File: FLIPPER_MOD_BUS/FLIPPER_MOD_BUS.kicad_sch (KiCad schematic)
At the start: 15 parts, among them J1 Conn_01x02, J2 Conn_01x10_Socket, J3 Conn_01x08_Socket, U1 SP3485EN

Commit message: Flipper Mod Bus Silkcscreen Updated
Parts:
- removed D1: LED_Small, LED_SMD:LED_0603_1608Metric_Pad1.05x0.95mm_HandSolder, symbol Device:LED_Small
- removed R8: 1K, Resistor_SMD:R_0603_1608Metric_Pad0.98x0.95mm_HandSolder, symbol Device:R_Small
- C2: LCSC# (none) -> C14663; Proveedor MOUSER -> LCSC; manf# 0603F104Z160CT -> (none)
- J1: manf# --- -> TRT-02
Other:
- company: (none) -> Electronic Cats
- title: (none) -> Flippe ModBus
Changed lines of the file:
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@@
 (kicad_sch (version 20230121) (generator eeschema)
   (paper "A4")
+  (title_block
+    (title "Flippe ModBus")
+    (date "2024-01-22")
+    (rev "1.0")
+    (company "Electronic Cats")
+    (comment 1 "Roberto Arellano")
+  )
   (junction (at 26.67 23.622) (diameter 0) (color 0 0 0 0)
   )
@@
   (no_connect (at 45.72 94.996))
   (no_connect (at 45.72 100.076))
-  (wire (pts (xy 165.354 39.624) (xy 165.354 45.466))
-    (stroke (width 0) (type default))
-  )
   (wire (pts (xy 32.004 25.908) (xy 32.004 23.622))
     (stroke (width 0) (type default))
@@
     (stroke (width 0) (type default))
   )
-  (wire (pts (xy 165.354 19.558) (xy 165.354 23.876))
-    (stroke (width 0) (type default))
-  )
   (wire (pts (xy 130.556 27.178) (xy 125.476 27.178))
     (stroke (width 0) (type default))
@@
   )
   (wire (pts (xy 21.336 23.622) (xy 26.67 23.622))
-    (stroke (width 0) (type default))
-  )
-  (wire (pts (xy 165.354 28.956) (xy 165.354 34.544))
     (stroke (width 0) (type default))
   )
@@
     )
   )
-  (symbol (lib_id "power:GND") (at 165.354 45.466 0) (mirror y) (unit 1)
-    (in_bom yes) (on_board yes) (dnp no)
-    (property "Reference" "#PWR09" (at 165.354 51.816 0)
-      (effects (font (size 1.27 1.27)) hide)
-    )
-    (property "Value" "GND" (at 165.227 49.8602 0)
-      (effects (font (size 1.27 1.27)))
-    )
-    (property "Footprint" "" (at 165.354 45.466 0)
-      (effects (font (size 1.27 1.27)) hide)
-    )
-    (property "Datasheet" "" (at 165.354 45.466 0)
-      (effects (font (size 1.27 1.27)) hide)
-    )
-    (pin "1")
-    (instances
-      (project "FLIPPER_MOD_BUS"
-        (path "/000d5789-2d2c-436e-a8f3-713f1968a92a"
-          (reference "#PWR09") (unit 1)
-        )
-      )
-    )
-  )
-  (symbol (lib_id "Device:LED_Small") (at 165.354 37.084 90) (unit 1)
-    (in_bom yes) (on_board yes) (dnp no) (fields_autoplaced)
-    (property "Reference" "D1" (at 167.386 35.7505 90)
-      (effects (font (size 1.27 1.27)) (justify right))
-    )
-    (property "Value" "LED_Small" (at 167.386 38.2905 90)
-      (effects (font (size 1.27 1.27)) (justify right))
-    )
-    (property "Footprint" "LED_SMD:LED_0603_1608Metric_Pad1.05x0.95mm_HandSolder" (at 165.354 37.084 90)
-      (effects (font (size 1.27 1.27)) hide)
-    )
-    (property "Datasheet" "~" (at 165.354 37.084 90)
-      (effects (font (size 1.27 1.27)) hide)
-    )
-    (pin "2")
-    (pin "1")
-    (instances
-      (project "FLIPPER_MOD_BUS"
-        (path "/000d5789-2d2c-436e-a8f3-713f1968a92a"
-          (reference "D1") (unit 1)
-        )
-      )
-    )
-  )
   (symbol (lib_id "Device:C_Small") (at 94.488 36.322 0) (unit 1)
     (in_bom yes) (on_board yes) (dnp no)
@@
       (effects (font (size 1.27 1.27)) hide)
     )
-    (property "manf#" "0603F104Z160CT" (at 94.488 36.322 0)
-      (effects (font (size 1.27 1.27)) hide)
-    )
-    (property "Proveedor" "MOUSER" (at 94.488 36.322 0)
+    (property "manf#" "" (at 94.488 36.322 0)
+      (effects (font (size 1.27 1.27)) hide)
+    )
+    (property "Proveedor" "LCSC" (at 94.488 36.322 0)
+      (effects (font (size 1.27 1.27)) hide)
+    )
+    (property "LCSC#" "C14663" (at 94.488 36.322 0)
       (effects (font (size 1.27 1.27)) hide)
     )
@@
     )
   )
-  (symbol (lib_id "power:+3.3V") (at 165.354 19.558 0) (mirror y) (unit 1)
-    (in_bom yes) (on_board yes) (dnp no)
-    (property "Reference" "#PWR08" (at 165.354 23.368 0)
-      (effects (font (size 1.27 1.27)) hide)
-    )
-    (property "Value" "+3.3V" (at 164.973 15.1638 0)
-      (effects (font (size 1.27 1.27)))
-    )
-    (property "Footprint" "" (at 165.354 19.558 0)
-      (effects (font (size 1.27 1.27)) hide)
-    )
-    (property "Datasheet" "" (at 165.354 19.558 0)
-      (effects (font (size 1.27 1.27)) hide)
-    )
-    (pin "1")
-    (instances
-      (project "FLIPPER_MOD_BUS"
-        (path "/000d5789-2d2c-436e-a8f3-713f1968a92a"
-          (reference "#PWR08") (unit 1)
-        )
-      )
-    )
-  )
   (symbol (lib_id "power:GND") (at 125.476 45.466 0) (mirror y) (unit 1)
     (in_bom yes) (on_board yes) (dnp no)
@@
       (effects (font (size 1.27 1.27)) hide)
     )
-    (property "manf#" "---" (at 135.636 32.004 0)
+    (property "manf#" "TRT-02" (at 135.636 32.004 0)
       (effects (font (size 1.27 1.27)) hide)
     )
@@
         )
       )
-    )
-  )
-  (symbol (lib_id "Device:R_Small") (at 165.354 26.416 0) (mirror x) (unit 1)
-    (in_bom yes) (on_board yes) (dnp no)
-    (property "Reference" "R8" (at 162.052 24.384 90)
-      (effects (font (size 1.27 1.27)) (justify left))
-    )
-    (property "Value" "1K" (at 163.576 24.638 90)
-      (effects (font (size 1.27 1.27)) (justify left))
-    )
-    (property "Footprint" "Resistor_SMD:R_0603_1608Metric_Pad0.98x0.95mm_HandSolder" (at 165.354 26.416 0)
-      (effects (font (size 1.27 1.27)) hide)
-    )
-    (property "Datasheet" "https://lcsc.com/product-detail/Chip-Resistor-Surface-Mount_UNI-ROYAL-Uniroyal-Elec-0603WAJ0203T5E_C25586.html" (at 165.354 26.416 0)
-      (effects (font (size 1.27 1.27)) hide)
-    )
-    (property "manf#" "0603WAJ0203T5E" (at 165.354 26.416 0)
-      (effects (font (size 1.27 1.27)) hide)
-    )
-    (property "LCSC#" "C25586" (at 165.354 26.416 0)
-      (effects (font (size 1.27 1.27)) hide)
-    )
-    (property "Proveedor" "LCSC" (at 165.354 26.416 0)
-      (effects (font (size 1.27 1.27)) hide)
-    )
-    (pin "1")
-    (pin "2")
-    (instances
-      (project "FLIPPER_MOD_BUS"
-        (path "/000d5789-2d2c-436e-a8f3-713f1968a92a"
-          (reference "R8") (unit 1)
-        )
-      )

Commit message: Flipper MODBUS Headers Updated
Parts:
- J2: footprint Connector_PinHeader_2.54mm:PinHeader_1x10_P2.54mm_Horizontal -> Connector_PinHeader_2.54mm:PinHeader_1x10_P2.54mm_Vertical; LCSC# C492418 -> C492409; manf# PZ254R-11-10P -> PZ254V-11-10P
- J3: footprint Connector_PinHeader_2.54mm:PinHeader_1x08_P2.54mm_Horizontal -> Connector_PinHeader_2.54mm:PinHeader_1x08_P2.54mm_Vertical; LCSC# C2894950 -> C492407; manf# PZ254-1-08-W-8.5 -> PZ254V-11-08P
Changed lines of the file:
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@@
       (effects (font (size 1.27 1.27)) (justify left))
     )
-    (property "Footprint" "Connector_PinHeader_2.54mm:PinHeader_1x08_P2.54mm_Horizontal" (at 81.28 104.902 0)
+    (property "Footprint" "Connector_PinHeader_2.54mm:PinHeader_1x08_P2.54mm_Vertical" (at 81.28 104.902 0)
       (effects (font (size 1.27 1.27)) hide)
     )
@@
       (effects (font (size 1.27 1.27)) hide)
     )
-    (property "manf#" "PZ254-1-08-W-8.5" (at 81.28 104.902 0)
-      (effects (font (size 1.27 1.27)) hide)
-    )
-    (property "LCSC#" "C2894950" (at 81.28 104.902 0)
+    (property "manf#" "PZ254V-11-08P" (at 81.28 104.902 0)
+      (effects (font (size 1.27 1.27)) hide)
+    )
+    (property "LCSC#" "C492407" (at 81.28 104.902 0)
       (effects (font (size 1.27 1.27)) hide)
     )
@@
       (effects (font (size 1.27 1.27)) (justify left))
     )
-    (property "Footprint" "Connector_PinHeader_2.54mm:PinHeader_1x10_P2.54mm_Horizontal" (at 50.8 102.616 0)
+    (property "Footprint" "Connector_PinHeader_2.54mm:PinHeader_1x10_P2.54mm_Vertical" (at 50.8 102.616 0)
       (effects (font (size 1.27 1.27)) hide)
     )
@@
       (effects (font (size 1.27 1.27)) hide)
     )
-    (property "LCSC#" "C492418" (at 50.8 102.616 0)
+    (property "LCSC#" "C492409" (at 50.8 102.616 0)
       (effects (font (size 1.27 1.27)) hide)
     )
@@
       (effects (font (size 1.27 1.27)) hide)
     )
-    (property "manf#" "PZ254R-11-10P" (at 50.8 102.616 0)
-      (effects (font (size 1.27 1.27)) hide)
-    )
+    (property "manf#" "PZ254V-11-10P" (at 50.8 102.616 0)
+      (effects (font (size 1.27 1.27)) hide)
+    )

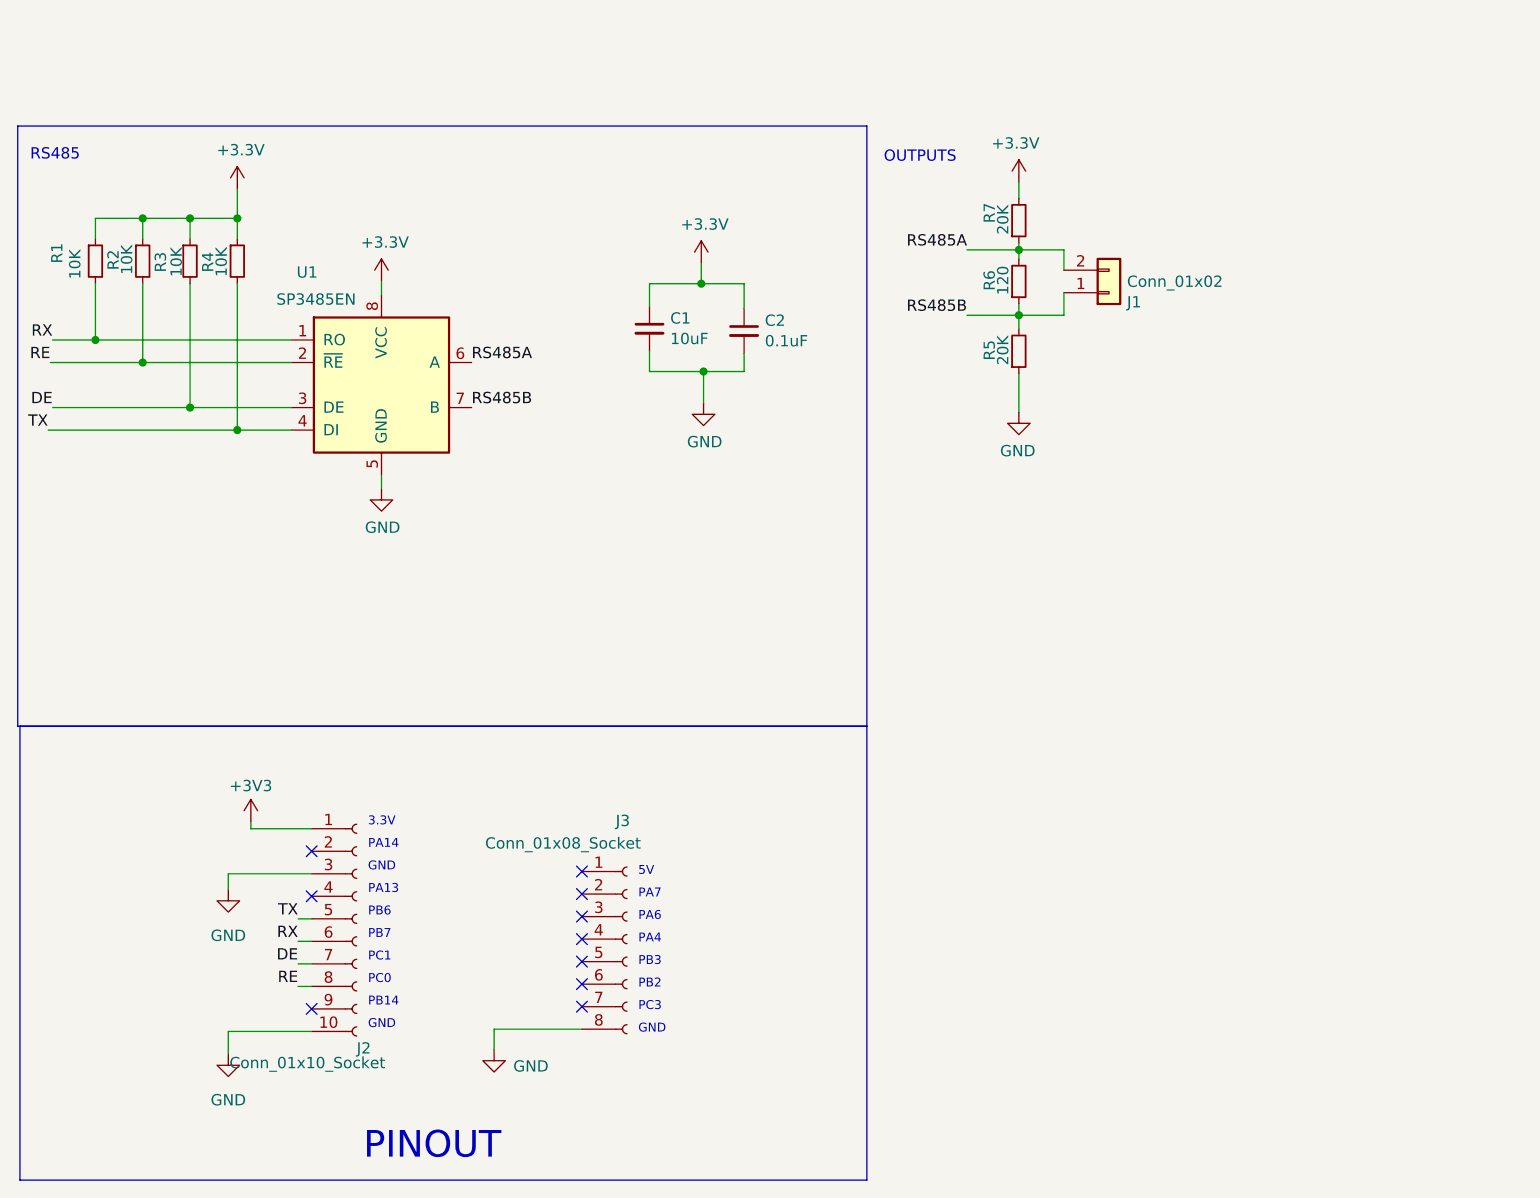
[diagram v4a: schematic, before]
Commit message: fix(hw): DE RE Pull Down & Jumper
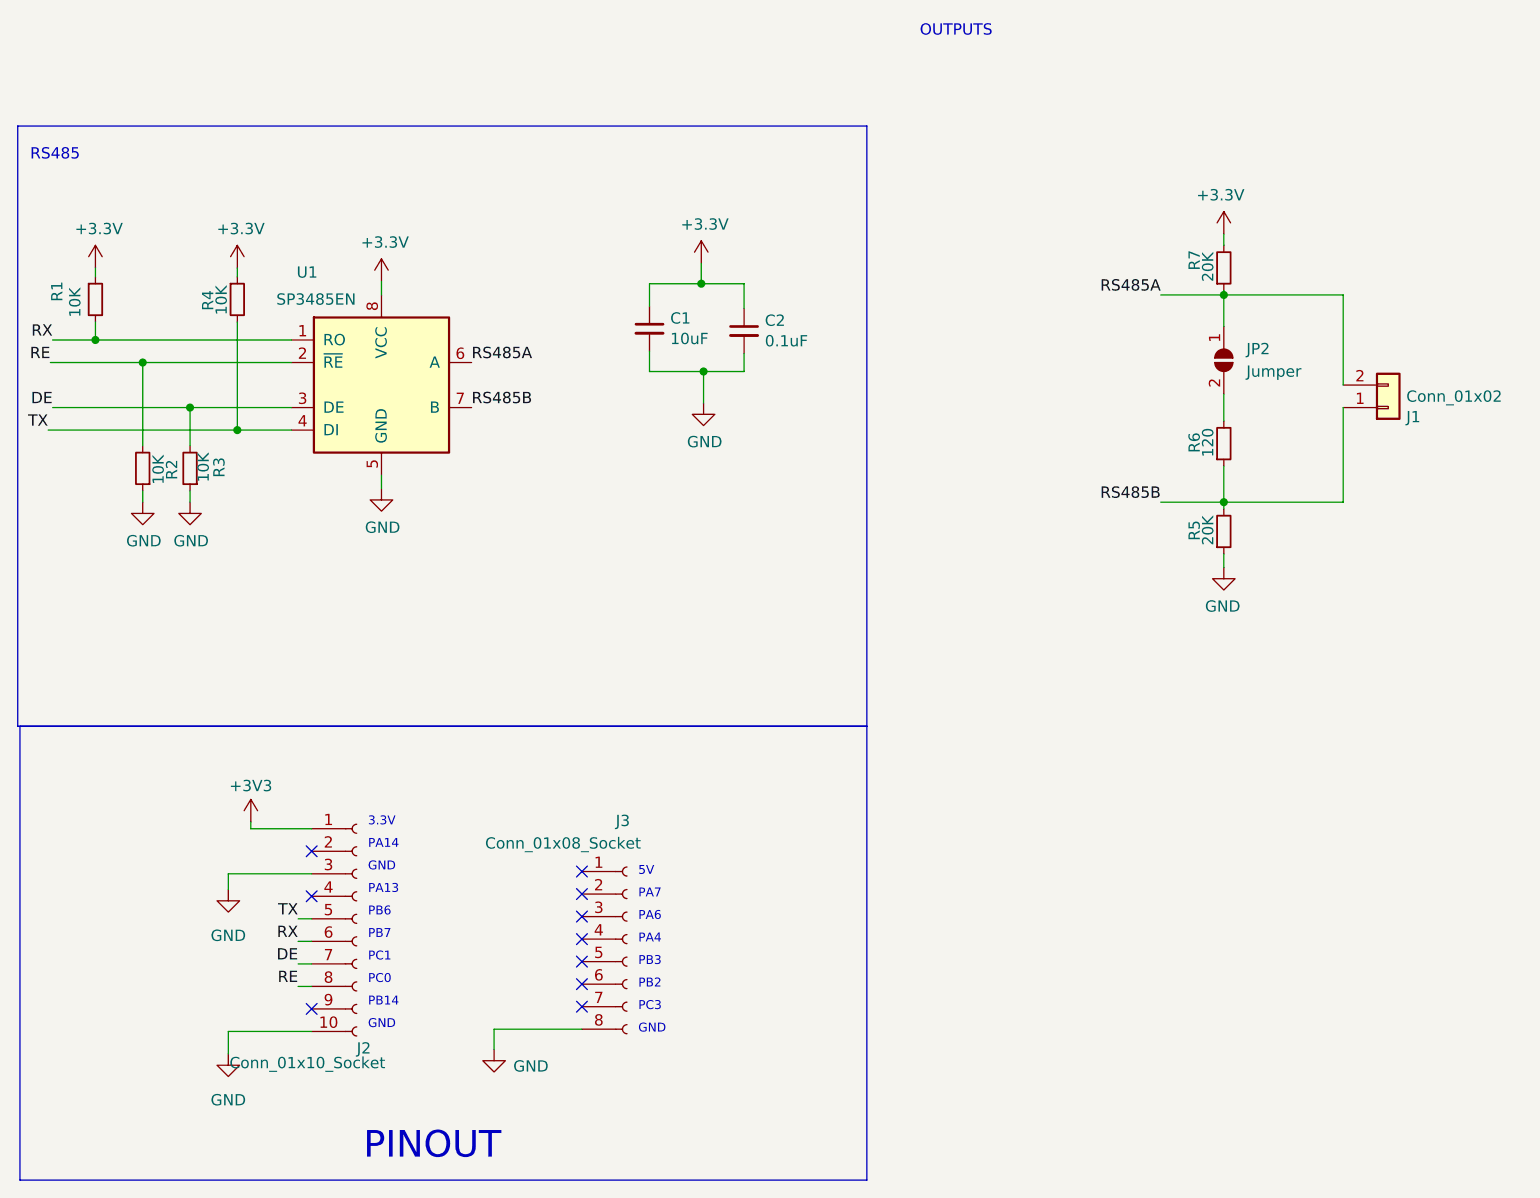
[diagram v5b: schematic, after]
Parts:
- added JP2: Jumper, Jumper:SolderJumper-2_P1.3mm_Open_TrianglePad1.0x1.5mm, symbol Jumper:SolderJumper_2_Open
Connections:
- net +3V3: no longer R2.1, R3.1
- net GND: now also R2.1, R3.1
- net RS485A: now also JP2.1 (A); no longer R6.2
- new net: JP2.2 (B), R6.2
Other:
- moved on the sheet: J1, R1, R2, R3, R4, R5, R6, R7

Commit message: fix(hw): Jumpers & version Updated
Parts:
- removed JP2: Jumper, Jumper:SolderJumper-2_P1.3mm_Open_TrianglePad1.0x1.5mm, symbol Jumper:SolderJumper_2_Open
- added J4: Conn_01x02_Socket, Connector_PinHeader_2.54mm:PinHeader_1x02_P2.54mm_Vertical, symbol Connector:Conn_01x02_Socket
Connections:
- net RS485A: now also J4.1 (Pin_1)
- net at R6.2: now also J4.2 (Pin_2)
